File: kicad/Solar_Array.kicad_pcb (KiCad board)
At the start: 2 copper layers, 31 x 22.9 mm, 26 parts, among them IC1 SPV1040, P1 PV_CELL, P2 CONN_01X07, Q1 Q_NPN_BCE, U1 LTC2990

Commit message: Updated Design Rules, generated new gerb files. -Fixed issues with soldermask relief. -Fixed issues with pad relief. -Regenerated f.paste, b.paste, f.mask, b.mask gerber files -
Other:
- rule pad_to_mask_clearance: 0.2 -> 0.001
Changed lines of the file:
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@@
   (page A4)
   (layers
-    (0 F.Cu signal)
+    (0 F.Cu signal hide)
     (31 B.Cu signal hide)
-    (32 B.Adhes user)
-    (33 F.Adhes user)
-    (34 B.Paste user)
+    (32 B.Adhes user hide)
+    (33 F.Adhes user hide)
+    (34 B.Paste user hide)
     (35 F.Paste user)
-    (36 B.SilkS user)
-    (37 F.SilkS user)
-    (38 B.Mask user)
-    (39 F.Mask user)
-    (40 Dwgs.User user)
-    (41 Cmts.User user)
-    (42 Eco1.User user)
-    (43 Eco2.User user)
-    (44 Edge.Cuts user)
-    (45 Margin user)
-    (46 B.CrtYd user)
-    (47 F.CrtYd user)
-    (48 B.Fab user)
-    (49 F.Fab user)
+    (36 B.SilkS user hide)
+    (37 F.SilkS user hide)
+    (38 B.Mask user hide)
+    (39 F.Mask user hide)
+    (40 Dwgs.User user hide)
+    (41 Cmts.User user hide)
+    (42 Eco1.User user hide)
+    (43 Eco2.User user hide)
+    (44 Edge.Cuts user hide)
+    (45 Margin user hide)
+    (46 B.CrtYd user hide)
+    (47 F.CrtYd user hide)
+    (48 B.Fab user hide)
+    (49 F.Fab user hide)
   )
   (setup
@@
     (pad_size 1.524 1.524)
     (pad_drill 0.762)
-    (pad_to_mask_clearance 0.2)
+    (pad_to_mask_clearance 0.001)
+    (solder_mask_min_width 0.001)
     (aux_axis_origin 0 0)
     (visible_elements FFFFFF7F)
     (pcbplotparams
-      (layerselection 0x01030_80000001)
+      (layerselection 0x00088_00000000)
       (usegerberextensions false)
       (excludeedgelayer true)
-      (linewidth 0.100000)
+      (linewidth 0.020000)
       (plotframeref false)
       (viasonmask false)

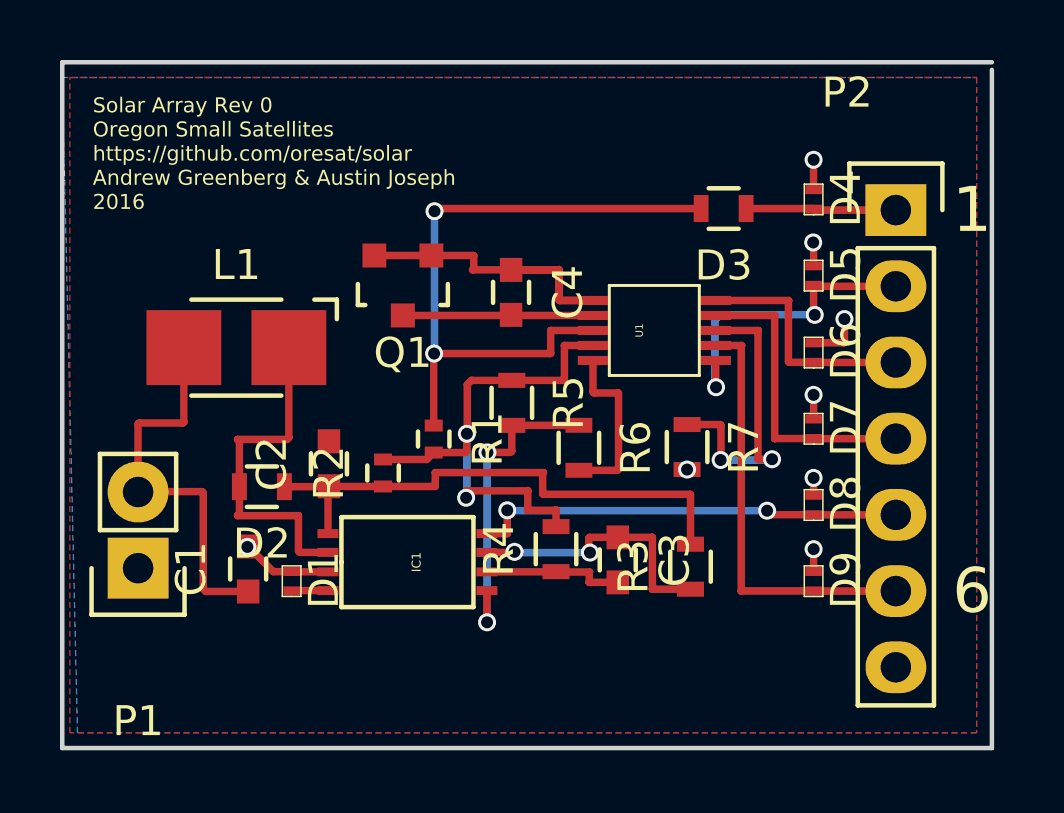
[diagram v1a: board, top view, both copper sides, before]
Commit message: Fixed glaring errors in layout.  Changed footprints.
-Fixed LTC2990 and SPV1040 footprints to reflect phsical layout
-Fixed board layout to accomodate actual design.
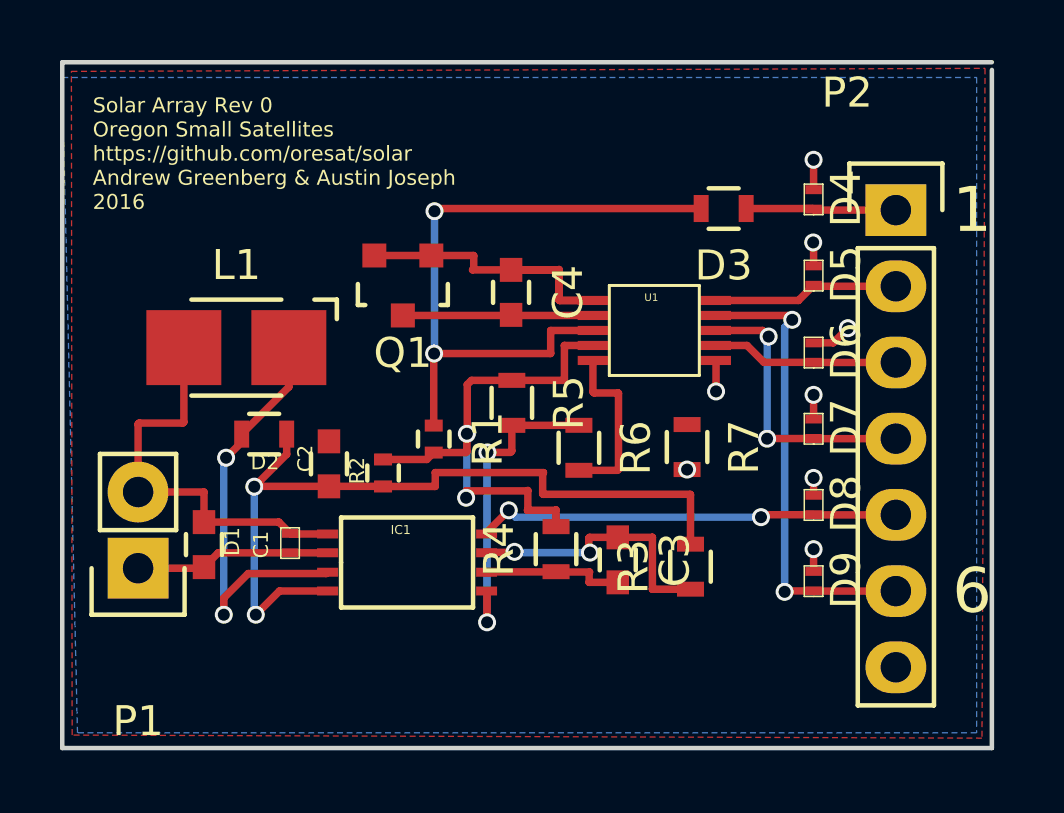
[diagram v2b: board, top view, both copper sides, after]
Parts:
- moved D2 1.75 mm to (136.5, 99.8)
- moved C1 1.68 mm to (134.5, 103.5), turned to 270 degrees
- moved D1 1.27 mm to (137.4, 103.4), turned to 270 degrees
- turned IC1 to 0 degrees
- turned U1 to 0 degrees
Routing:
- net Net-(R7-Pad1): track 10.2 -> 0.00 mm, vias 2 -> 0
- net Net-(C2-Pad1): track 18.0 -> 26.7 mm, vias 0 -> 2
- net GND: track 14.7 -> 18.8 mm
- net Net-(D5-Pad1): track 10.3 -> 6.23 mm, vias 2 -> 0
- net Net-(D2-Pad2): track 11.6 -> 14.2 mm, vias 0 -> 2
- net Net-(D6-Pad1): track 8.07 -> 6.24 mm
- net Net-(D9-Pad1): track 14.2 -> 15.5 mm, vias 0 -> 2
- net Net-(C1-Pad1): track 14.5 -> 13.8 mm
- net Net-(D7-Pad1): track 10.1 -> 9.57 mm, vias 0 -> 2

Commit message: Added test points.  Removed Shotkey.
-Added test points to PVin, VCC and Vout.
-Removed potentially uneccesary shotkey diodes.
-Increased width of SPV1040 pads.
-Generally cleaned up traces on board.
-Updated 3d Model of various footprints in Solar Libs.
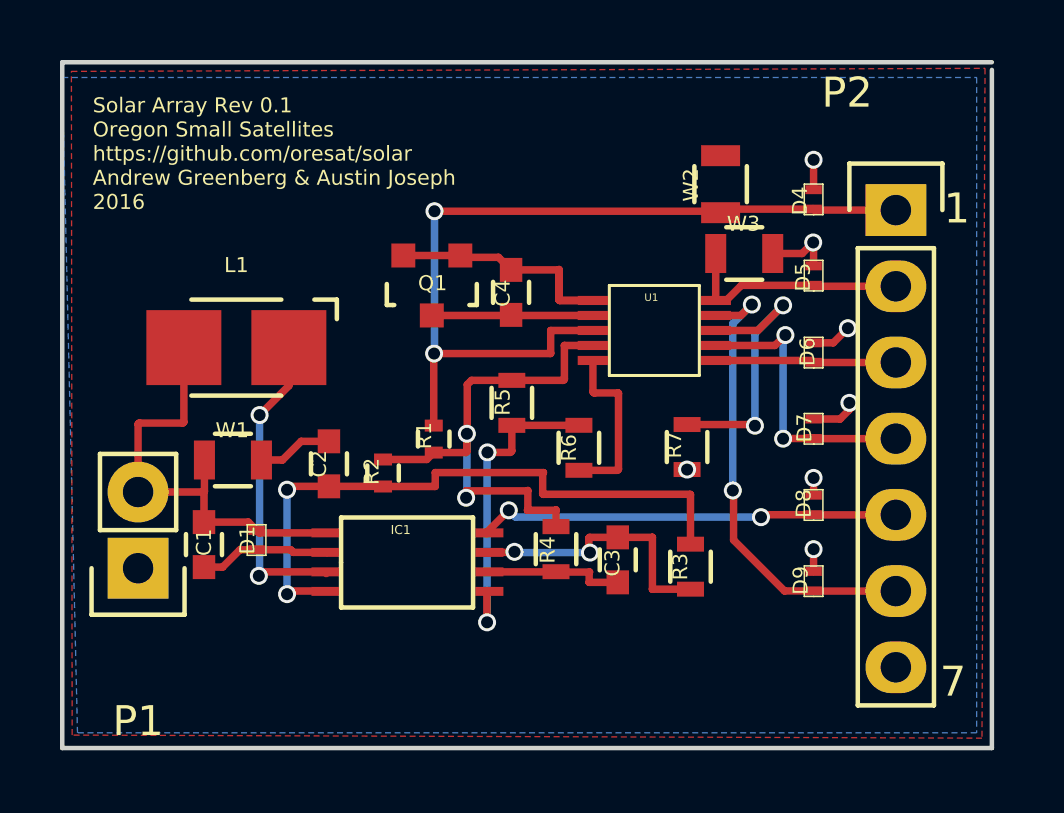
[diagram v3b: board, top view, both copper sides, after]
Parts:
- removed D2, D3: D_Schottky, Resistors_SMD:R_0603
- added W1: TEST, Test_Point, F.Cu at (135.5, 100.6)
- added W2: TEST, Solar:Test_Point, F.Cu at (151.7, 91.4)
- added W3: TEST, Solar:Test_Point, F.Cu at (152.5, 93.8)
- IC1: footprint Solar:TSSOP-8 -> TSSOP-8
- L1: footprint Inductors:Inductor_1212 -> Inductor_1212
- R2: value .007 -> .1
- U1: footprint Solar:MSOP-10 -> MSOP-10
- moved D1 1.12 mm to (136.3, 103.3)
- moved Q1 0.97 mm to (142.1, 94.8)
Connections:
- D4 pad 1: Net-(D3-Pad1) -> Net-(D4-Pad1)
- P2 pad 1: Net-(D3-Pad1) -> Net-(D4-Pad1)
- R1 pad 1: Net-(D3-Pad2) -> Net-(D4-Pad1)
- U1 pad 3: Net-(D3-Pad2) -> Net-(D4-Pad1)
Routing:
- net Net-(D4-Pad1): track 0.00 -> 28.7 mm, vias 0 -> 2
- net Net-(D3-Pad2): track 22.1 -> 0.00 mm, vias 2 -> 0
- net Net-(R7-Pad1): track 0.00 -> 9.27 mm, vias 0 -> 2
- net Net-(C2-Pad1): track 26.7 -> 21.3 mm
- net Net-(D3-Pad1): track 5.01 -> 0.00 mm
- net Net-(IC1-Pad3): track 14.2 -> 11.3 mm
- net Net-(C4-Pad1): track 12.6 -> 9.69 mm
- net Net-(D5-Pad1): track 6.23 -> 7.79 mm
- net GND: track 18.8 -> 20.3 mm, vias 8 -> 7
- net Net-(C1-Pad1): track 13.8 -> 14.8 mm
- net Net-(C4-Pad2): track 6.34 -> 5.36 mm
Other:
- board text added: "7"
- board text added: "Solar Array Rev 0.1 Oregon Small Satellites https://github.com/oresat/solar Andrew Greenberg & Austin Joseph 2016"
- board text removed: "6"
- board text removed: "Solar Array Rev 0 Oregon Small Satellites https://github.com/oresat/solar Andrew Greenberg & Austin Joseph 2016"

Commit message: Added ground tacks.
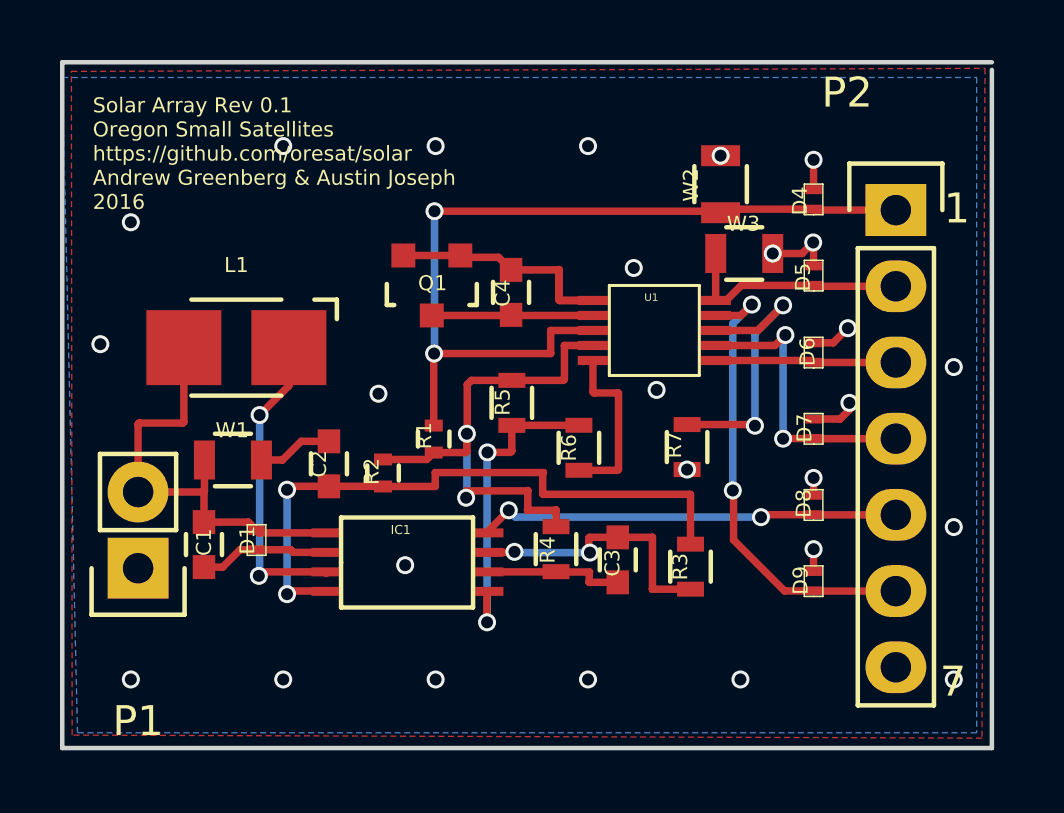
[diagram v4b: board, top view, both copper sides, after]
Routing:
- net GND: track 20.3 -> 20.4 mm, vias 7 -> 26
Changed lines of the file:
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@@
     (links 57)
     (no_connects 1)
-    (area 129.718999 87.300999 160.857001 110.311001)
+    (area 129.718999 87.300999 160.964334 110.311001)
     (thickness 1.6)
     (drawings 7)
-    (tracks 229)
+    (tracks 252)
     (zones 0)
     (modules 27)
@@
   (page A4)
   (layers
-    (0 F.Cu signal)
+    (0 F.Cu signal hide)
     (31 B.Cu signal)
     (32 B.Adhes user hide)
@@
   (segment (start 133.8479 99.3674) (end 133.8124 99.4029) (width 0.25) (layer F.Cu) (net 1))
   (segment (start 132.3213 101.7016) (end 132.334 101.6889) (width 0.25) (layer F.Cu) (net 1))
+  (via (at 141.224 104.14) (size 0.6) (drill 0.4) (layers F.Cu B.Cu) (net 2))
+  (via (at 131.064 96.774) (size 0.6) (drill 0.4) (layers F.Cu B.Cu) (net 2))
+  (via (at 159.512 97.536) (size 0.6) (drill 0.4) (layers F.Cu B.Cu) (net 2))
+  (via (at 159.512 102.87) (size 0.6) (drill 0.4) (layers F.Cu B.Cu) (net 2))
+  (via (at 159.512 107.95) (size 0.6) (drill 0.4) (layers F.Cu B.Cu) (net 2))
+  (via (at 148.844 94.234) (size 0.6) (drill 0.4) (layers F.Cu B.Cu) (net 2))
+  (via (at 149.606 98.298) (size 0.6) (drill 0.4) (layers F.Cu B.Cu) (net 2))
+  (via (at 140.335 98.425) (size 0.6) (drill 0.4) (layers F.Cu B.Cu) (net 2))
+  (via (at 137.16 90.17) (size 0.6) (drill 0.4) (layers F.Cu B.Cu) (net 2))
+  (via (at 142.24 90.17) (size 0.6) (drill 0.4) (layers F.Cu B.Cu) (net 2))
+  (via (at 147.32 90.17) (size 0.6) (drill 0.4) (layers F.Cu B.Cu) (net 2))
+  (via (at 153.477 93.7514) (size 0.6) (drill 0.4) (layers F.Cu B.Cu) (net 2) (status C00000))
+  (segment (start 154.4574 93.7514) (end 154.8257 93.3831) (width 0.25) (layer F.Cu) (net 2))
+  (segment (start 154.8384 94.163) (end 154.8384 93.3958) (width 0.25) (layer F.Cu) (net 2))
+  (via (at 154.8257 93.3831) (size 0.6) (drill 0.4) (layers F.Cu B.Cu) (net 2))
+  (segment (start 154.8384 93.3958) (end 154.8257 93.3831) (width 0.25) (layer F.Cu) (net 2))
+  (segment (start 153.477 93.7514) (end 154.4574 93.7514) (width 0.25) (layer F.Cu) (net 2))
+  (segment (start 153.4516 93.726) (end 153.416 93.726) (width 0.25) (layer B.Cu) (net 2))
+  (segment (start 153.477 93.7514) (end 153.4516 93.726) (width 0.25) (layer B.Cu) (net 2) (status 400000))
+  (via (at 151.7396 90.49) (size 0.6) (drill 0.4) (layers F.Cu B.Cu) (net 2) (status C00000))
+  (segment (start 151.765 90.4875) (end 151.7421 90.4875) (width 0.25) (layer B.Cu) (net 2))
+  (segment (start 151.7421 90.4875) (end 151.7396 90.49) (width 0.25) (layer B.Cu) (net 2) (status 800000))
+  (via (at 132.08 92.71) (size 0.6) (drill 0.4) (layers F.Cu B.Cu) (net 2))
+  (via (at 132.08 107.95) (size 0.6) (drill 0.4) (layers F.Cu B.Cu) (net 2))
+  (via (at 137.16 107.95) (size 0.6) (drill 0.4) (layers F.Cu B.Cu) (net 2))
+  (via (at 142.24 107.95) (size 0.6) (drill 0.4) (layers F.Cu B.Cu) (net 2))
+  (via (at 147.32 107.95) (size 0.6) (drill 0.4) (layers F.Cu B.Cu) (net 2))
+  (via (at 152.4 107.95) (size 0.6) (drill 0.4) (layers F.Cu B.Cu) (net 2))
   (segment (start 136.4336 100.6348) (end 137.1346 100.6348) (width 0.25) (layer F.Cu) (net 2))
   (segment (start 137.7576 100.0118) (end 138.684 100.0118) (width 0.25) (layer F.Cu) (net 2))
@@
   (segment (start 135.7174 103.6268) (end 137.4088 103.6268) (width 0.25) (layer F.Cu) (net 2))
   (segment (start 135.14 104.2042) (end 135.7174 103.6268) (width 0.25) (layer F.Cu) (net 2))
-  (segment (start 153.477 93.7514) (end 154.4574 93.7514) (width 0.25) (layer F.Cu) (net 2))
-  (segment (start 154.8384 93.3958) (end 154.8257 93.3831) (width 0.25) (layer F.Cu) (net 2))
-  (via (at 154.8257 93.3831) (size 0.6) (drill 0.4) (layers F.Cu B.Cu) (net 2))
-  (segment (start 154.8384 93.3958) (end 154.8384 94.163) (width 0.25) (layer F.Cu) (net 2))
-  (segment (start 154.4574 93.7514) (end 154.8257 93.3831) (width 0.25) (layer F.Cu) (net 2))
   (segment (start 154.8384 99.2684) (end 155.7222 99.2684) (width 0.25) (layer F.Cu) (net 2))
   (via (at 156.0322 98.7298) (size 0.6) (drill 0.4) (layers F.Cu B.Cu) (net 2))

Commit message: Regenerated gerberfiles
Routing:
- net GND: track 20.4 -> 115.8 mm, vias 26 -> 23
- net Net-(D4-Pad1): track 28.7 -> 28.8 mm, vias 2 -> 3
- net Net-(C1-Pad1): track 14.8 -> 14.9 mm, vias 0 -> 1
- net Net-(D5-Pad1): track 7.79 -> 7.87 mm, vias 0 -> 1
